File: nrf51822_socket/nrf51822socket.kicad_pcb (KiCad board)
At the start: 2 copper layers, 14 parts, among them J1 Teste analógico, J2 Esquerdo, J3 Direito, J4 Enable LDO, J5 Input Output, Q1 Q_NMOS_GSD, U1 LN1134

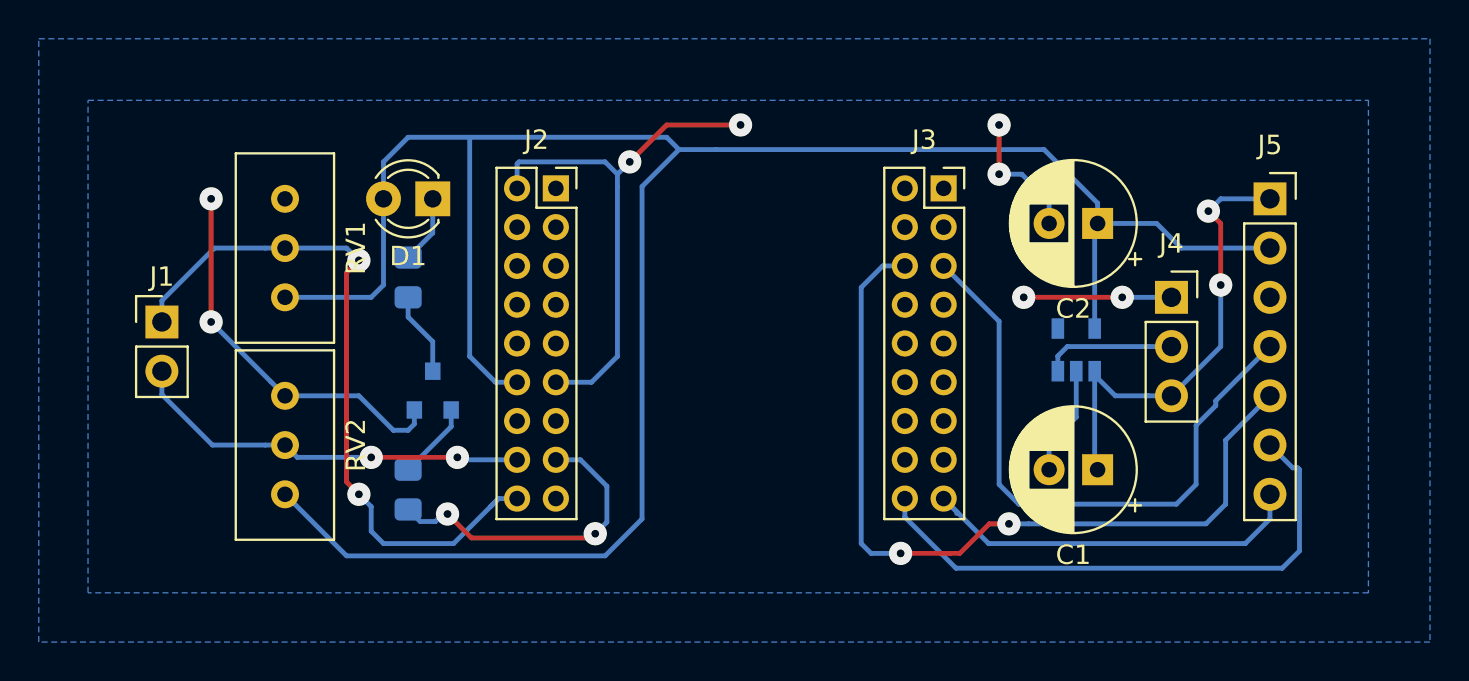
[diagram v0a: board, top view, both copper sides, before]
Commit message: V 0.2 do socket NRF51822 - esquematico e layout
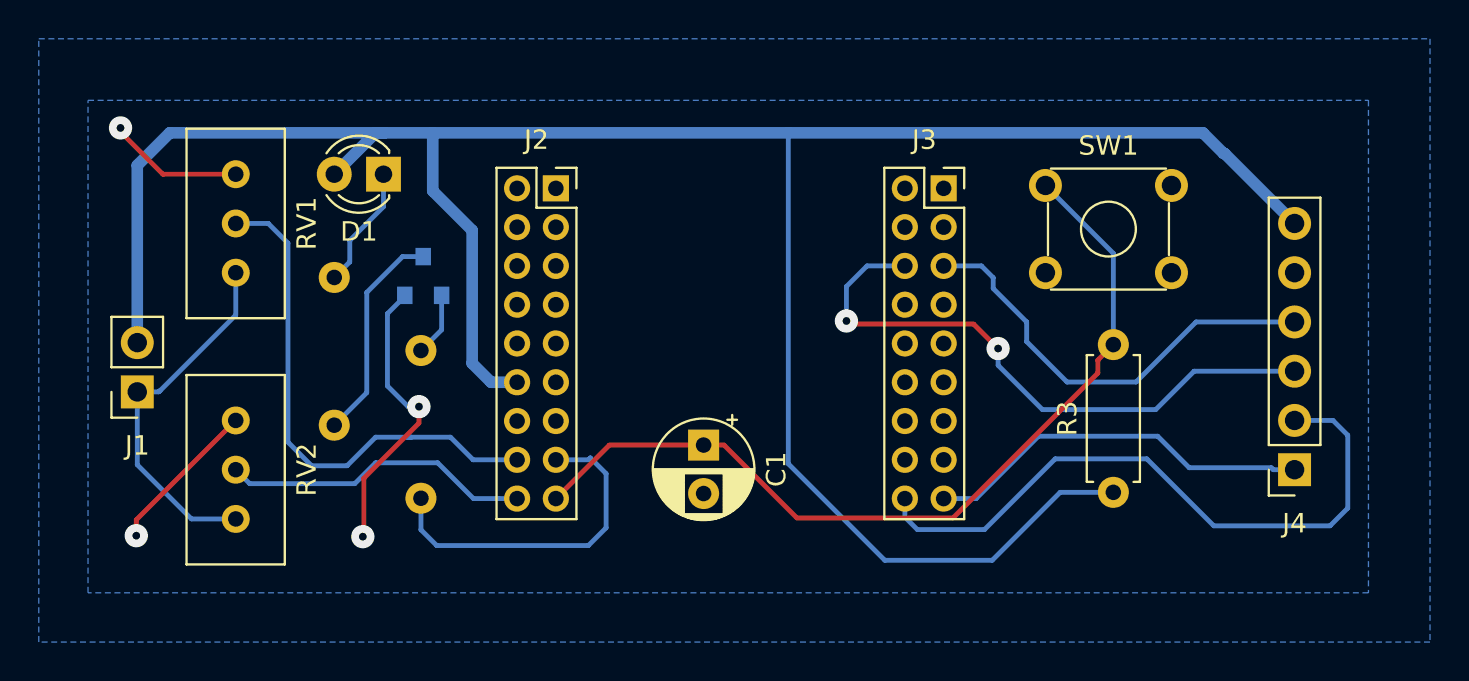
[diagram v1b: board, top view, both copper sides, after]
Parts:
- removed C2: 1 uF, Capacitor_THT:CP_Radial_D6.3mm_P2.50mm
- removed J5: Input Output, Connector_PinSocket_2.54mm:PinSocket_1x07_P2.54mm_Vertical
- removed U1: LN1134, Package_TO_SOT_SMD:SOT-23-5
- added R3: 1M, Resistor_THT:R_Axial_DIN0207_L6.3mm_D2.5mm_P7.62mm_Horizontal, F.Cu at (135.9, 98.5)
- added SW1: SW_Push_Dual, Button_Switch_THT:SW_TH_Tactile_Omron_B3F-10xx, F.Cu at (132.4, 82.6)
- C1: value 1 uF -> 100nF; footprint Capacitor_THT:CP_Radial_D6.3mm_P2.50mm -> Capacitor_THT:CP_Radial_D5.0mm_P2.50mm
- J1: value Teste analógico -> Conn_01x02_Female; footprint Connector_PinHeader_2.54mm:PinHeader_1x02_P2.54mm_Vertical -> Connector_PinSocket_2.54mm:PinSocket_1x02_P2.54mm_Vertical
- J4: value Enable LDO -> Conn_01x06; footprint Connector_PinSocket_2.54mm:PinSocket_1x03_P2.54mm_Vertical -> Connector_PinSocket_2.54mm:PinSocket_1x06_P2.54mm_Vertical
- R1, R2: footprint Resistor_SMD:R_0805_2012Metric_Pad1.15x1.40mm_HandSolder -> Resistor_THT:R_Axial_DIN0207_L6.3mm_D2.5mm_P7.62mm_Horizontal
- moved C1 20.4 mm to (114.8, 96.0), turned to 270 degrees
- moved J4 10.9 mm to (145.3, 97.3), turned to 180 degrees
- moved Q1 5.93 mm to (100.3, 87.3)
- moved J1 3.82 mm to (85.6, 93.3), turned to 180 degrees
- moved R2 3.81 mm to (95.8, 87.4)
- moved RV1 2.84 mm to (90.7, 87.1)
- moved RV2 2.84 mm to (90.7, 99.8)
- moved D1 2.84 mm to (98.3, 82.0)
- moved R1 0.80 mm to (100.2, 98.8)
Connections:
- net Net-(J2-Pad15) renamed /02
- C1 pad 1: +5V -> /04
- J1 pad 2: Net-(J1-Pad2) -> +2V5
- J2 pad 1: (no net) -> Net-(J2-Pad1)
- J2 pad 10: (no net) -> Net-(J2-Pad10)
- J2 pad 13: (no net) -> Net-(J2-Pad13)
- J2 pad 14: (no net) -> Net-(J2-Pad14)
- J2 pad 16: Net-(J1-Pad2) -> /01
- J2 pad 17: (no net) -> /04
- J2 pad 18: Net-(J1-Pad1) -> Net-(J2-Pad18)
- J2 pad 3: (no net) -> Net-(J2-Pad3)
- J2 pad 4: (no net) -> Net-(J2-Pad4)
- J2 pad 5: (no net) -> Net-(J2-Pad5)
- J2 pad 6: (no net) -> Net-(J2-Pad6)
- J2 pad 7: (no net) -> Net-(J2-Pad7)
- J2 pad 8: (no net) -> Net-(J2-Pad8)
- J2 pad 9: (no net) -> Net-(J2-Pad9)
- J3 pad 1: (no net) -> Net-(J3-Pad1)
- J3 pad 10: (no net) -> Net-(J3-Pad10)
- J3 pad 11: (no net) -> Net-(J3-Pad11)
- J3 pad 12: (no net) -> Net-(J3-Pad12)
- J3 pad 13: (no net) -> Net-(J3-Pad13)
- J3 pad 14: (no net) -> Net-(J3-Pad14)
- J3 pad 15: (no net) -> Net-(J3-Pad15)
- J3 pad 16: (no net) -> Net-(J3-Pad16)
- J3 pad 2: (no net) -> Net-(J3-Pad2)
- J3 pad 3: (no net) -> Net-(J3-Pad3)
- J3 pad 4: (no net) -> Net-(J3-Pad4)
- J3 pad 7: (no net) -> Net-(J3-Pad7)
- J3 pad 8: (no net) -> Net-(J3-Pad8)
- J3 pad 9: (no net) -> Net-(J3-Pad9)
- J4 pad 1: GND -> RX
- J4 pad 2: Net-(J4-Pad2) -> TX
- J4 pad 3: +5V -> SWDIO
- RV1 pad 1: +2V5 -> Net-(J1-Pad1)
- RV1 pad 2: Net-(J1-Pad1) -> /01
- RV2 pad 1: +2V5 -> Net-(J1-Pad1)
- RV2 pad 2: Net-(J1-Pad2) -> Net-(J2-Pad18)
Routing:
- net /04: track 0.00 -> 45.2 mm
- net GND: track 67.4 -> 30.2 mm, vias 8 -> 4
- net /01: track 0.00 -> 27.0 mm
- net +5V: track 24.0 -> 0.00 mm, vias 2 -> 0
- net Net-(J1-Pad2): track 20.9 -> 0.00 mm, vias 2 -> 0
- net Net-(J1-Pad1): track 36.7 -> 18.9 mm, vias 2 -> 0
- net Net-(J2-Pad18): track 0.00 -> 16.0 mm
- net SWDIO: track 42.5 -> 31.6 mm
- net SWCLK: track 32.1 -> 22.8 mm
- net Net-(Q1-Pad3): track 4.34 -> 11.2 mm
- net Net-(J4-Pad2): track 6.84 -> 0.00 mm
- net +2V5: track 121.1 -> 127.7 mm
- net TX: track 29.0 -> 34.2 mm
- net Net-(D1-Pad1): track 3.56 -> 6.38 mm
- net /02: track 16.6 -> 17.7 mm, vias 2 -> 0
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
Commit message: algumas melhorias
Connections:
- J2 pad 1: Net-(J2-Pad1) -> (no net)
- J2 pad 10: Net-(J2-Pad10) -> (no net)
- J2 pad 13: Net-(J2-Pad13) -> (no net)
- J2 pad 14: Net-(J2-Pad14) -> (no net)
- J2 pad 3: Net-(J2-Pad3) -> (no net)
- J2 pad 4: Net-(J2-Pad4) -> (no net)
- J2 pad 5: Net-(J2-Pad5) -> (no net)
- J2 pad 6: Net-(J2-Pad6) -> (no net)
- J2 pad 7: Net-(J2-Pad7) -> (no net)
- J2 pad 8: Net-(J2-Pad8) -> (no net)
- J2 pad 9: Net-(J2-Pad9) -> (no net)
- J3 pad 1: Net-(J3-Pad1) -> (no net)
- J3 pad 10: Net-(J3-Pad10) -> (no net)
- J3 pad 11: Net-(J3-Pad11) -> (no net)
- J3 pad 12: Net-(J3-Pad12) -> (no net)
- J3 pad 13: Net-(J3-Pad13) -> (no net)
- J3 pad 14: Net-(J3-Pad14) -> (no net)
- J3 pad 15: Net-(J3-Pad15) -> (no net)
- J3 pad 16: Net-(J3-Pad16) -> (no net)
- J3 pad 2: Net-(J3-Pad2) -> (no net)
- J3 pad 3: Net-(J3-Pad3) -> (no net)
- J3 pad 4: Net-(J3-Pad4) -> (no net)
- J3 pad 7: Net-(J3-Pad7) -> (no net)
- J3 pad 8: Net-(J3-Pad8) -> (no net)
- J3 pad 9: Net-(J3-Pad9) -> (no net)
- SW1 pad 2: GND -> (no net)
- SW1 pad 3: Net-(SW1-Pad3) -> (no net)
- SW1 pad 4: Net-(SW1-Pad4) -> GND
